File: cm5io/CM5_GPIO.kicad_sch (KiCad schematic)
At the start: 14 parts, among them J14 JST_SHBM04B-SRSS-TB, J3 Conn_01x03, J7 Micro_SD_Card_Det, SW1 Right angle Tact button, U18 RT9742GGJ5, U5 74LVC1G07SE-7

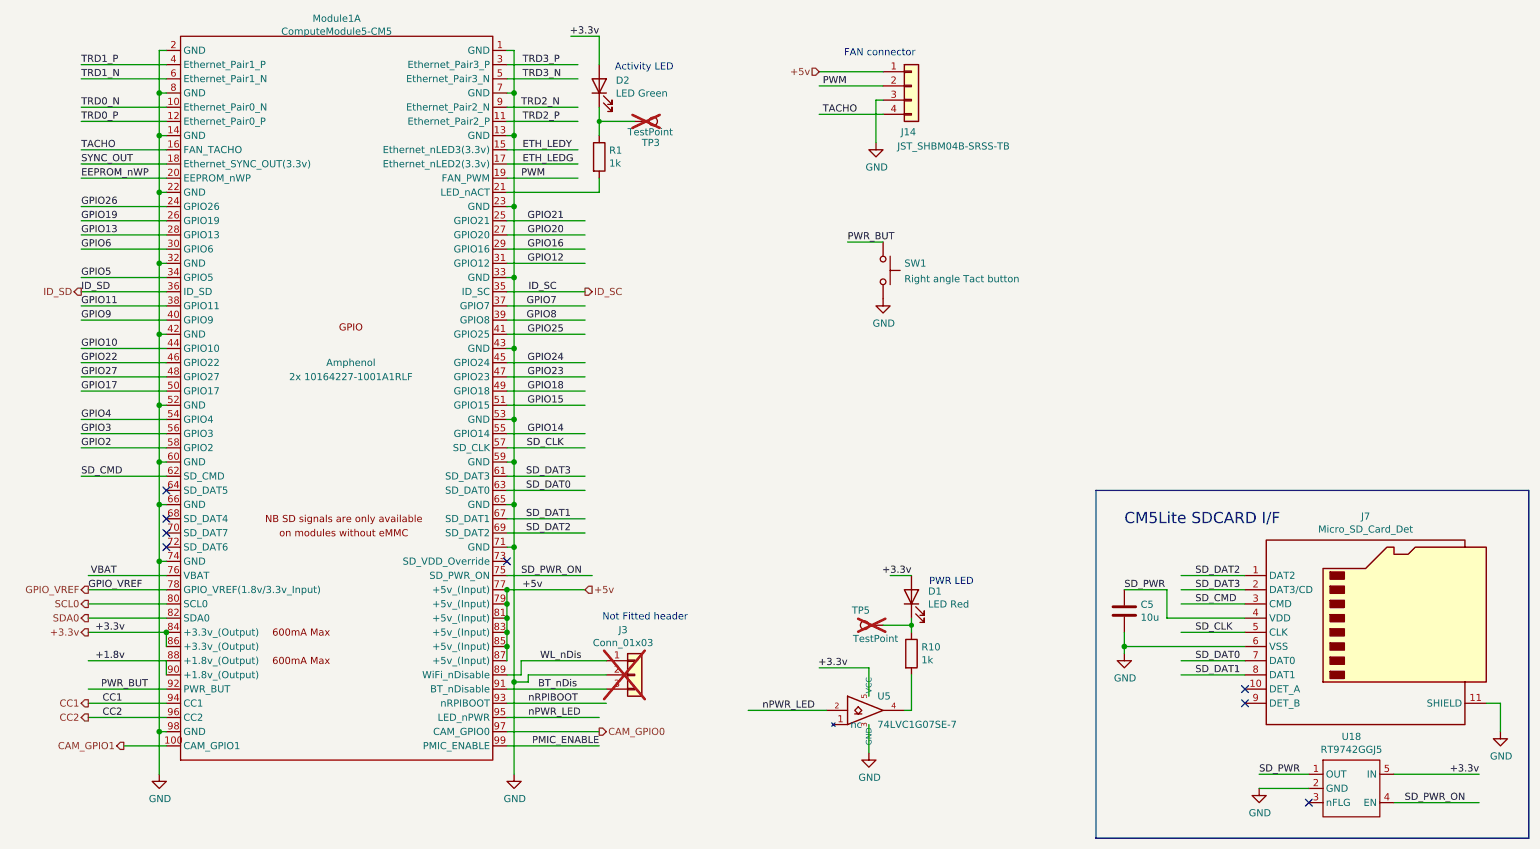
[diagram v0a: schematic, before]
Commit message: [cm5io] remove USB-C and NVMe connectors, clean up routing
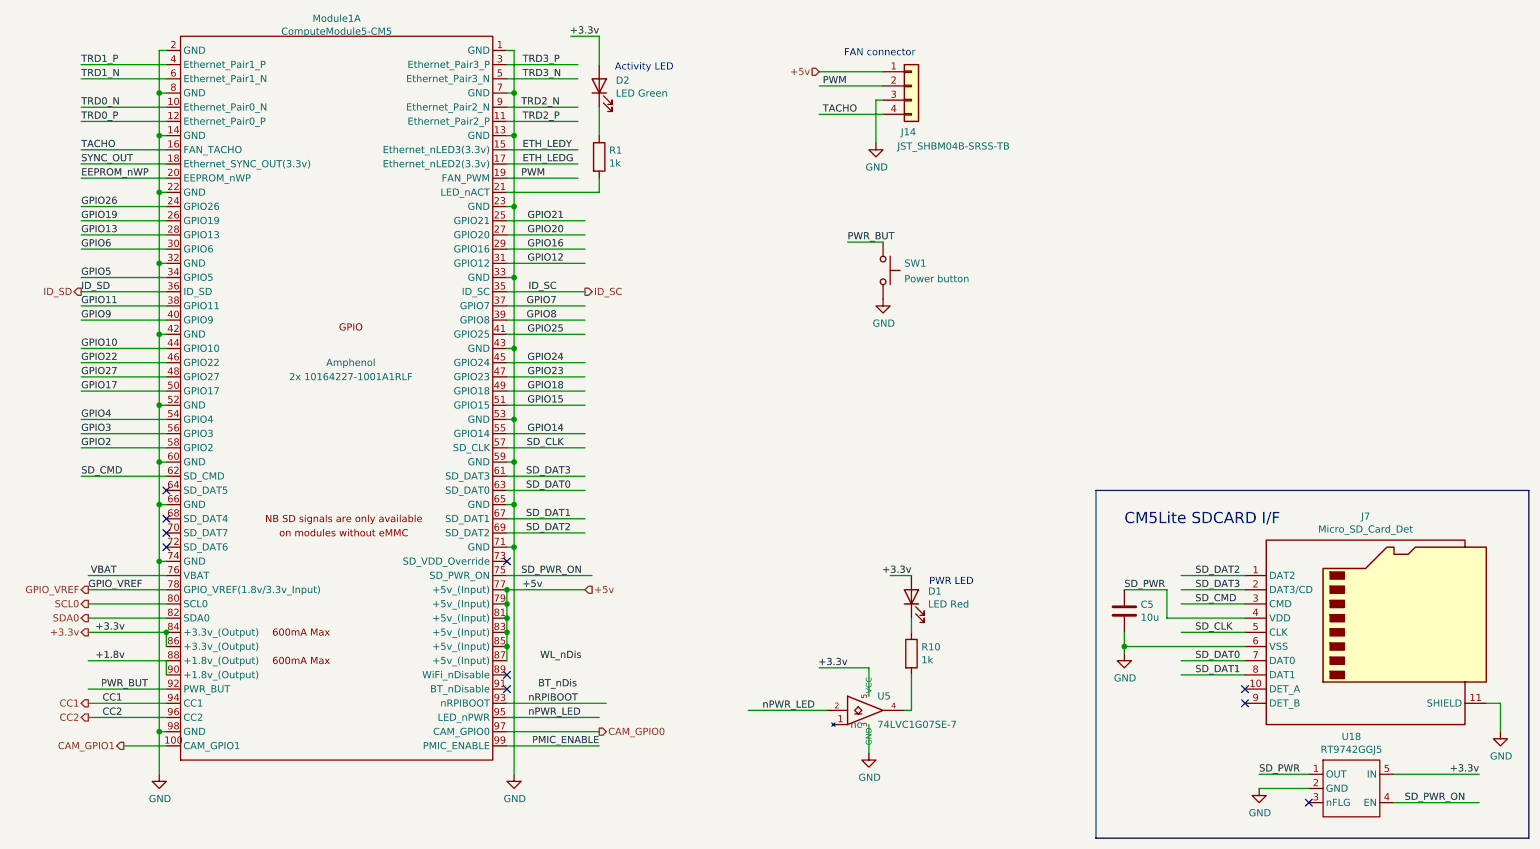
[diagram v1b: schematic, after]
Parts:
- removed J3: Conn_01x03, Connector_PinHeader_2.54mm:PinHeader_1x03_P2.54mm_Vertical, symbol Connector_Generic:Conn_01x03
- removed TP3, TP5: TestPoint, TestPoint:TestPoint_Pad_2.0x2.0mm, symbol Connector:TestPoint
- SW1: value Right angle Tact button -> Power button
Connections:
- net BT_nDis: no longer Module1.91 (BT_nDisable)
- net WL_nDis: no longer Module1.89 (WiFi_nDisable)
- no-connect marks 8 -> 10
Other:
- note removed: "Not Fitted header"
